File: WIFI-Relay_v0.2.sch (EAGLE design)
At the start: 38 parts, among them CN1 PBS-3-VERTICAL, CN2 PBS-2-VERTICAL, CN3 PBS-8-1.27-VERTICAL, CN4 PBS-8-1.27-VERTICAL, CN5 PBS-2-VERTICAL, CN6 PBS-2-VERTICAL, CN7 PBS-4-VERTICAL, IC1 74LS595D, IC2 74LS595D, IC3 MC34063AD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

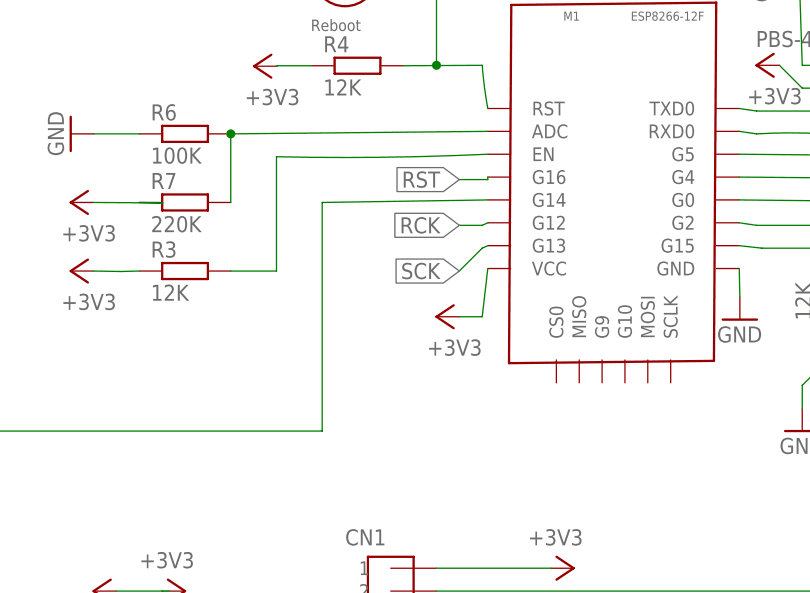
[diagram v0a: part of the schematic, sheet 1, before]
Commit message: Button "Reset settings" was replaced with N$27
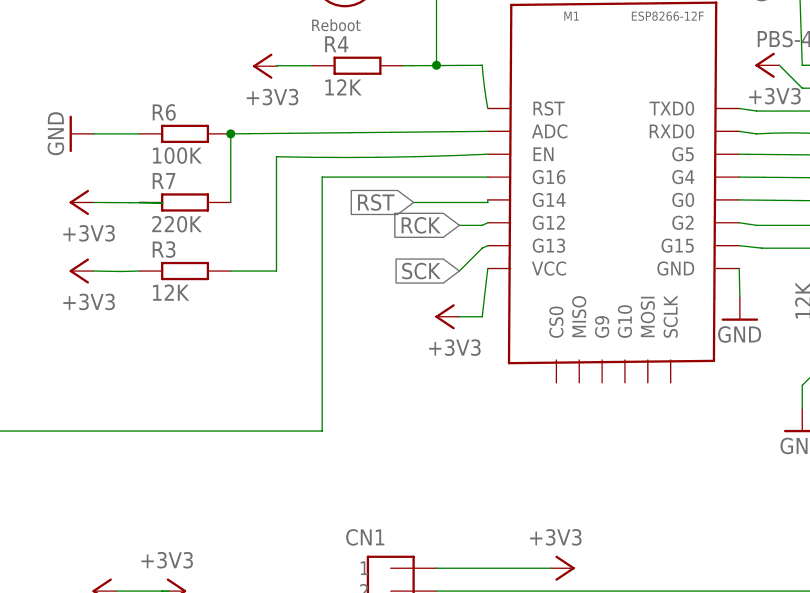
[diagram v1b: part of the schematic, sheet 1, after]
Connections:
- net N$27: now also M1.G16; no longer M1.G14
- net RST: now also M1.G14; no longer M1.G16
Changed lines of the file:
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@@
 <segment>
 <pinref part="IC1" gate="A" pin="SER"/>
-<pinref part="M1" gate="G$1" pin="G14"/>
-<wire x1="-12.08" y1="-4.8" x2="-30.48" y2="-5.08" width="0.1524" layer="91"/>
-<wire x1="-30.48" y1="-5.08" x2="-30.48" y2="-30.48" width="0.1524" layer="91"/>
+<wire x1="-30.48" y1="-2.26" x2="-30.48" y2="-30.48" width="0.1524" layer="91"/>
 <wire x1="-30.48" y1="-30.48" x2="-86.36" y2="-30.48" width="0.1524" layer="91"/>
+<pinref part="M1" gate="G$1" pin="G16"/>
+<wire x1="-30.48" y1="-2.26" x2="-12.08" y2="-2.26" width="0.1524" layer="91"/>
 </segment>
 </net>
@@
 <net name="RST" class="0">
 <segment>
-<pinref part="M1" gate="G$1" pin="G16"/>
-<wire x1="-12.08" y1="-2.26" x2="-12.08" y2="-2.54" width="0.1524" layer="91"/>
-<wire x1="-12.08" y1="-2.54" x2="-15.24" y2="-2.54" width="0.1524" layer="91"/>
-<label x="-15.24" y="-2.54" size="1.778" layer="95" rot="R180" xref="yes"/>
+<label x="-20.32" y="-5.08" size="1.778" layer="95" rot="R180" xref="yes"/>
+<pinref part="M1" gate="G$1" pin="G14"/>
+<wire x1="-12.08" y1="-4.8" x2="-12.08" y2="-5.08" width="0.1524" layer="91"/>
+<wire x1="-12.08" y1="-5.08" x2="-20.32" y2="-5.08" width="0.1524" layer="91"/>
 </segment>
 <segment>
